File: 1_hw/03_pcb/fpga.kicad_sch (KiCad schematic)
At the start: 23 parts, among them U12 ICE40UP5K-SG48ITR

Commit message: MINOR: Added Board Rules & Constraints.
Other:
- note removed: "TB: GO THROUGH HW CHECKLIST!"
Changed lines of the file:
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@@
-		)
-	)
-	(text "TB: GO THROUGH HW CHECKLIST!"
-		(exclude_from_sim no)
-		(at 167.64 33.02 0)
-		(effects
-			(font
-				(size 1.27 1.27)
-				(color 255 0 0 1)
-			)
 		)
 	)

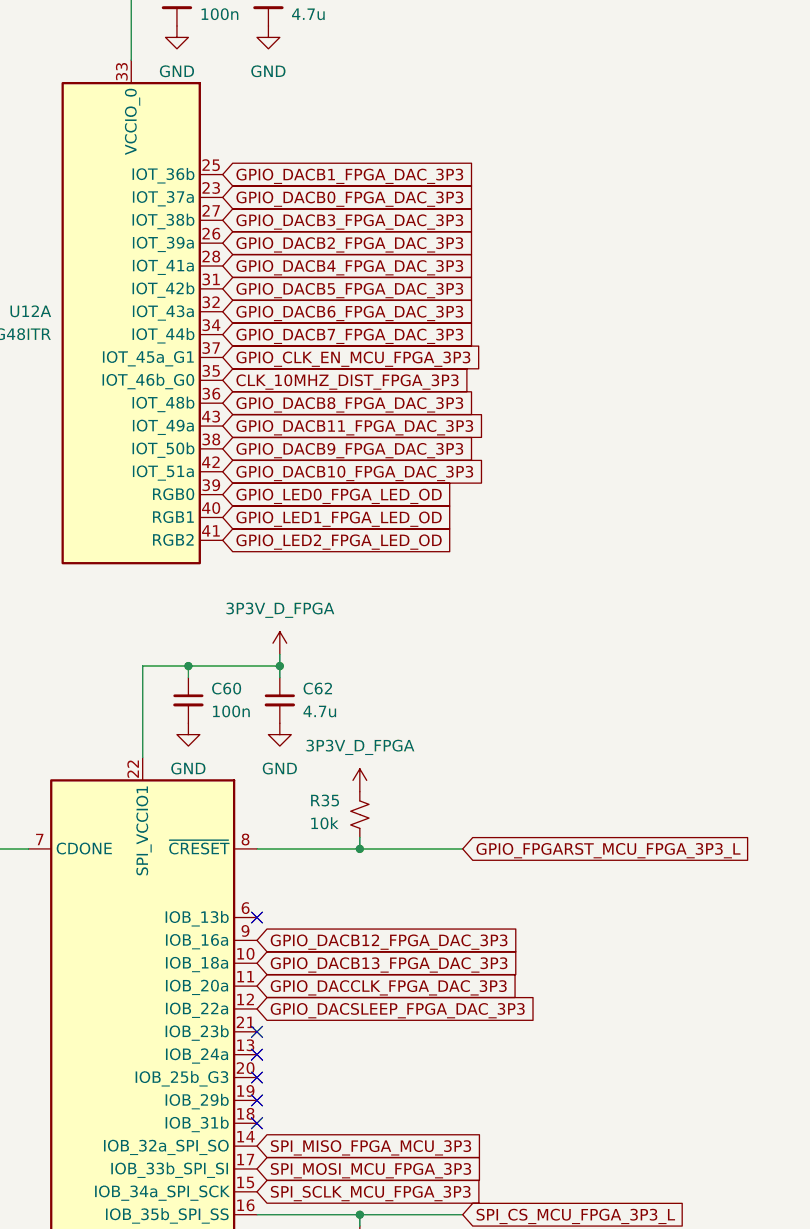
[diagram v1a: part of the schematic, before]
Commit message: FEAT: Started FPGA Layout, 1/2 Complete.
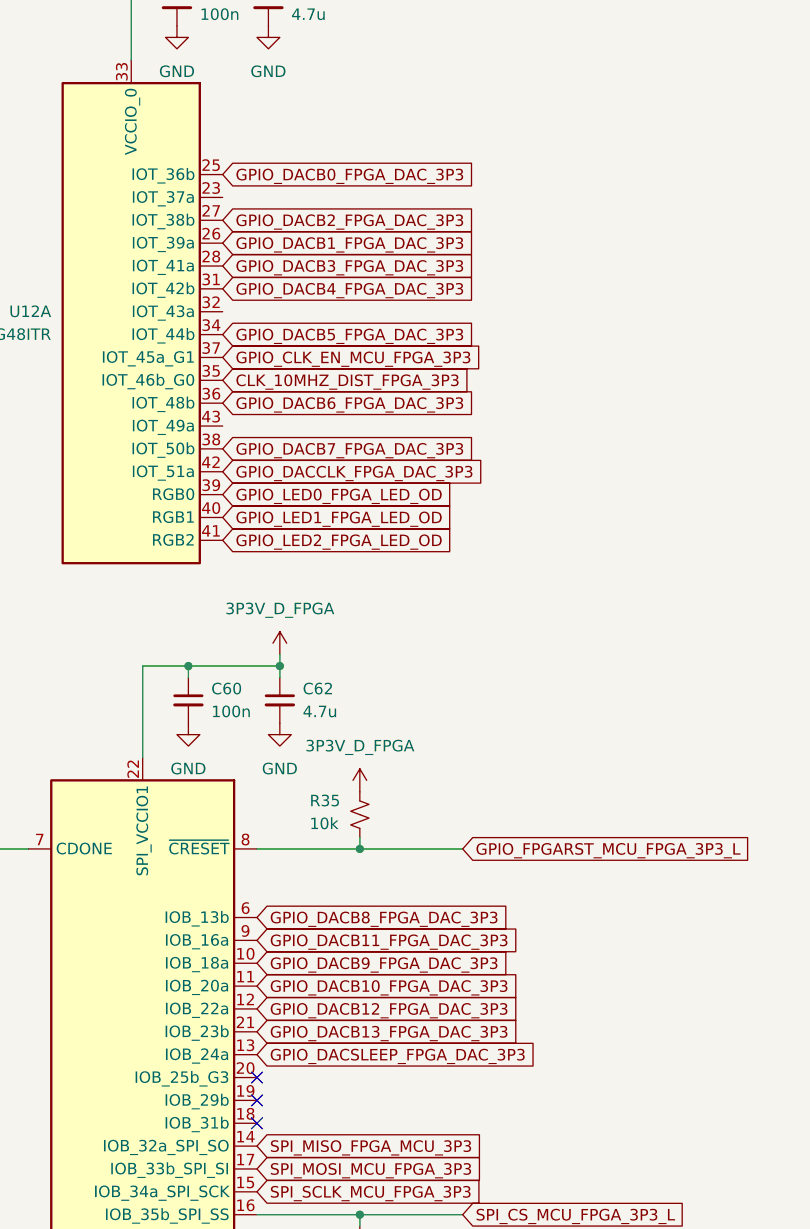
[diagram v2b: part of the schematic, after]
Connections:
- net GPIO_DACB0_FPGA_DAC_3P3: now also U12.25 (IOT_36b); no longer U12.23 (IOT_37a)
- net GPIO_DACB10_FPGA_DAC_3P3: now also U12.11 (IOB_20a); no longer U12.42 (IOT_51a)
- net GPIO_DACB11_FPGA_DAC_3P3: now also U12.9 (IOB_16a); no longer U12.43 (IOT_49a)
- net GPIO_DACB12_FPGA_DAC_3P3: now also U12.12 (IOB_22a); no longer U12.9 (IOB_16a)
- net GPIO_DACB13_FPGA_DAC_3P3: now also U12.21 (IOB_23b); no longer U12.10 (IOB_18a)
- net GPIO_DACB1_FPGA_DAC_3P3: now also U12.26 (IOT_39a); no longer U12.25 (IOT_36b)
- net GPIO_DACB2_FPGA_DAC_3P3: now also U12.27 (IOT_38b); no longer U12.26 (IOT_39a)
- net GPIO_DACB3_FPGA_DAC_3P3: now also U12.28 (IOT_41a); no longer U12.27 (IOT_38b)
- net GPIO_DACB4_FPGA_DAC_3P3: now also U12.31 (IOT_42b); no longer U12.28 (IOT_41a)
- net GPIO_DACB5_FPGA_DAC_3P3: now also U12.34 (IOT_44b); no longer U12.31 (IOT_42b)
- net GPIO_DACB6_FPGA_DAC_3P3: now also U12.36 (IOT_48b); no longer U12.32 (IOT_43a)
- net GPIO_DACB7_FPGA_DAC_3P3: now also U12.38 (IOT_50b); no longer U12.34 (IOT_44b)
- net GPIO_DACB8_FPGA_DAC_3P3: now also U12.6 (IOB_13b); no longer U12.36 (IOT_48b)
- net GPIO_DACB9_FPGA_DAC_3P3: now also U12.10 (IOB_18a); no longer U12.38 (IOT_50b)
- net GPIO_DACCLK_FPGA_DAC_3P3: now also U12.42 (IOT_51a); no longer U12.11 (IOB_20a)
- net GPIO_DACSLEEP_FPGA_DAC_3P3: now also U12.13 (IOB_24a); no longer U12.12 (IOB_22a)
- no-connect marks 14 -> 11

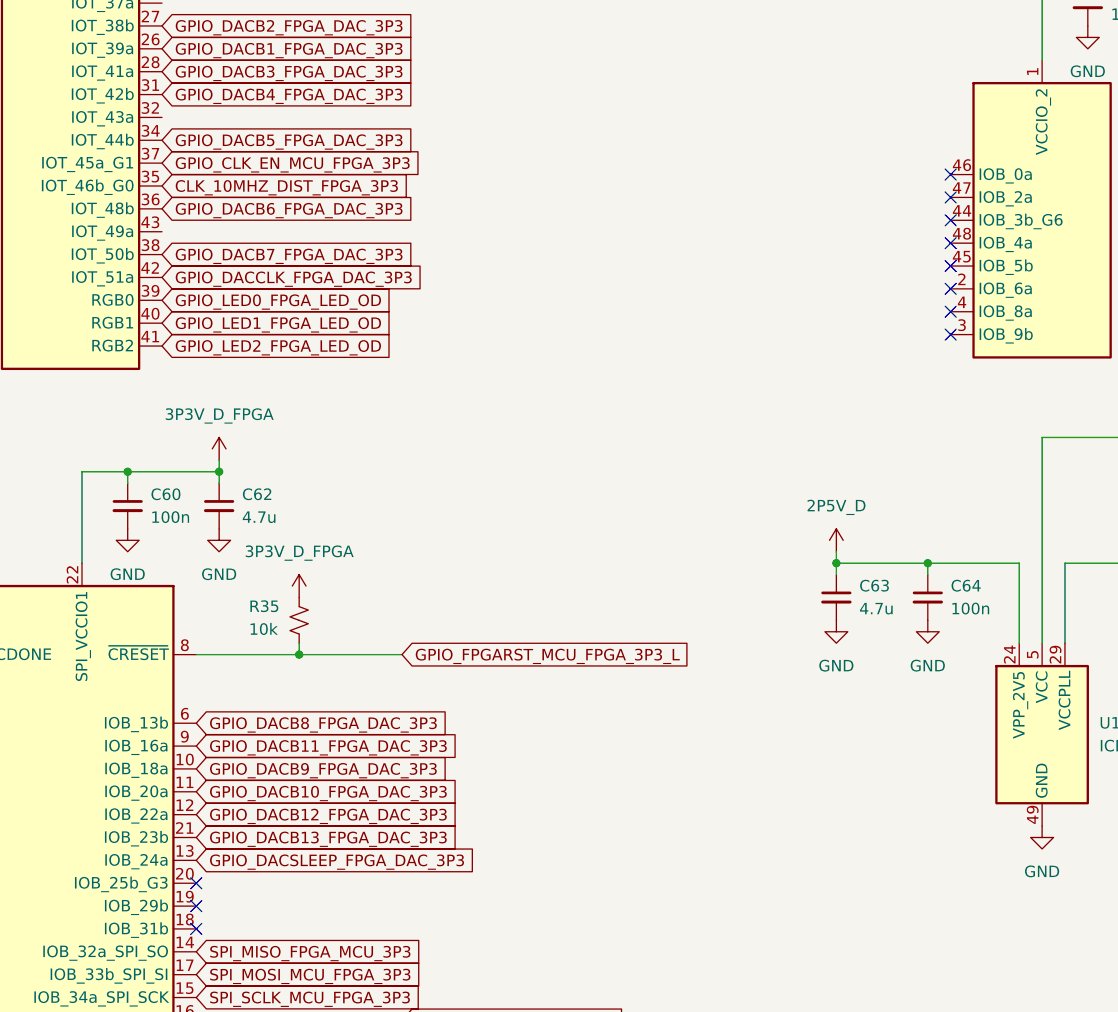
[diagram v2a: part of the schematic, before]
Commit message: FEAT: Completed FPGA Layout.
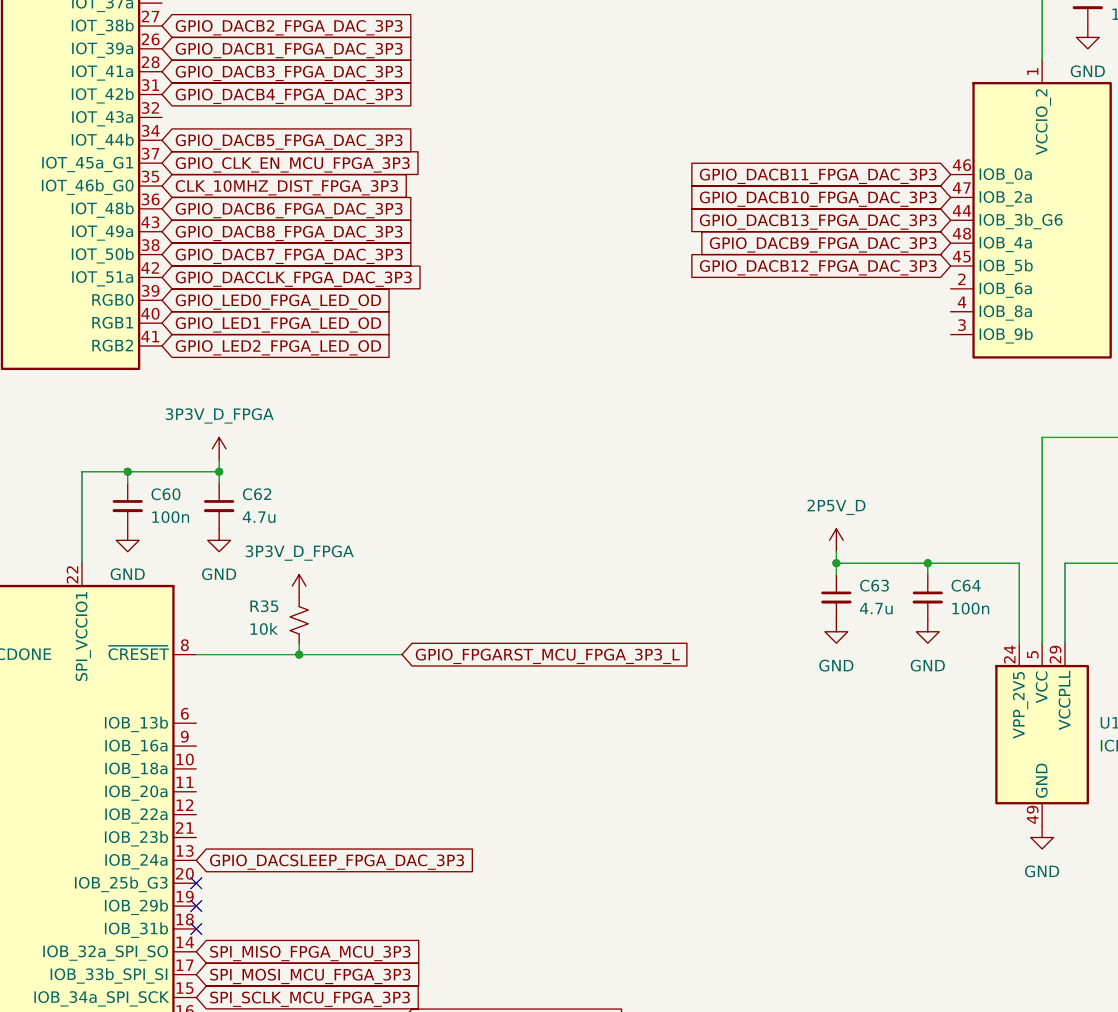
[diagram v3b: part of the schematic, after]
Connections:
- net GPIO_DACB10_FPGA_DAC_3P3: now also U12.47 (IOB_2a); no longer U12.11 (IOB_20a)
- net GPIO_DACB11_FPGA_DAC_3P3: now also U12.46 (IOB_0a); no longer U12.9 (IOB_16a)
- net GPIO_DACB12_FPGA_DAC_3P3: now also U12.45 (IOB_5b); no longer U12.12 (IOB_22a)
- net GPIO_DACB13_FPGA_DAC_3P3: now also U12.44 (IOB_3b_G6); no longer U12.21 (IOB_23b)
- net GPIO_DACB8_FPGA_DAC_3P3: now also U12.43 (IOT_49a); no longer U12.6 (IOB_13b)
- net GPIO_DACB9_FPGA_DAC_3P3: now also U12.48 (IOB_4a); no longer U12.10 (IOB_18a)
- no-connect marks 11 -> 3
